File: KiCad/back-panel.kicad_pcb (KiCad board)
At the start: 2 copper layers, 93.3 x 69.3 mm, 4 parts

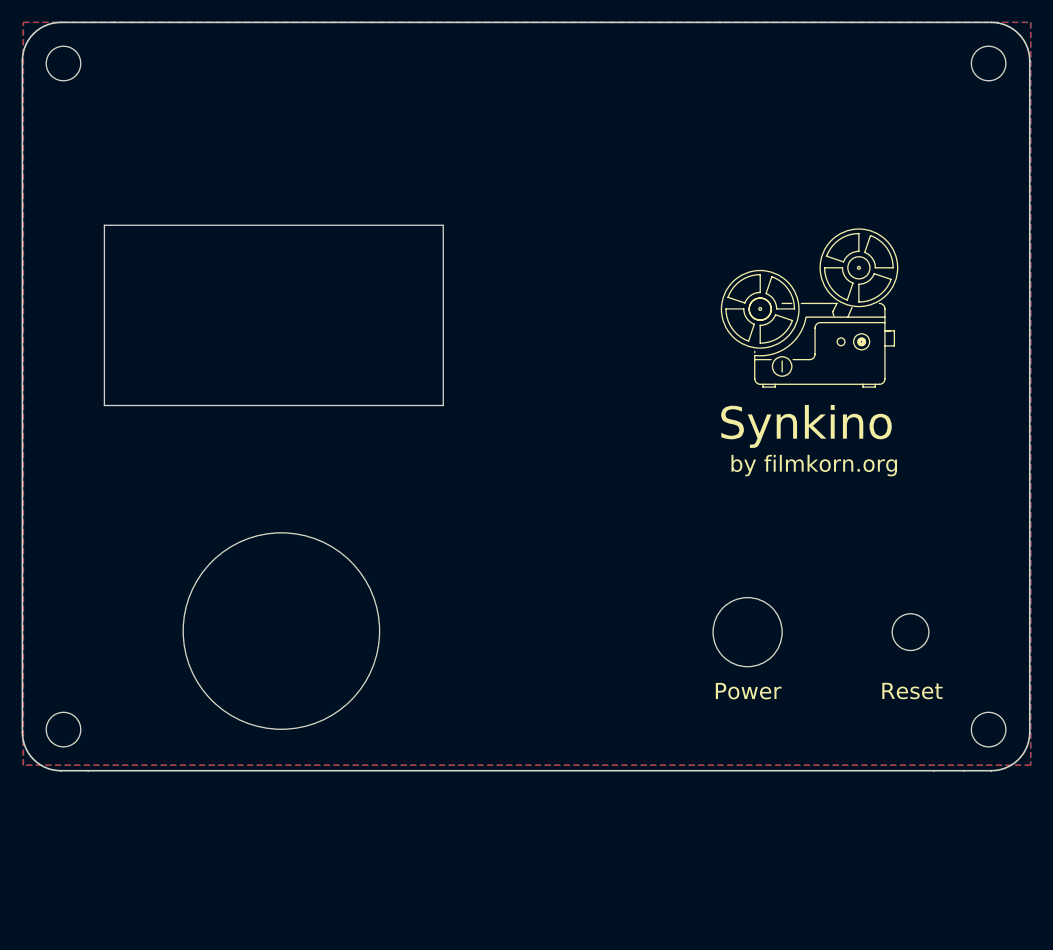
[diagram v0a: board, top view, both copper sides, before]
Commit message: Adding Battery Holder, Battery connector
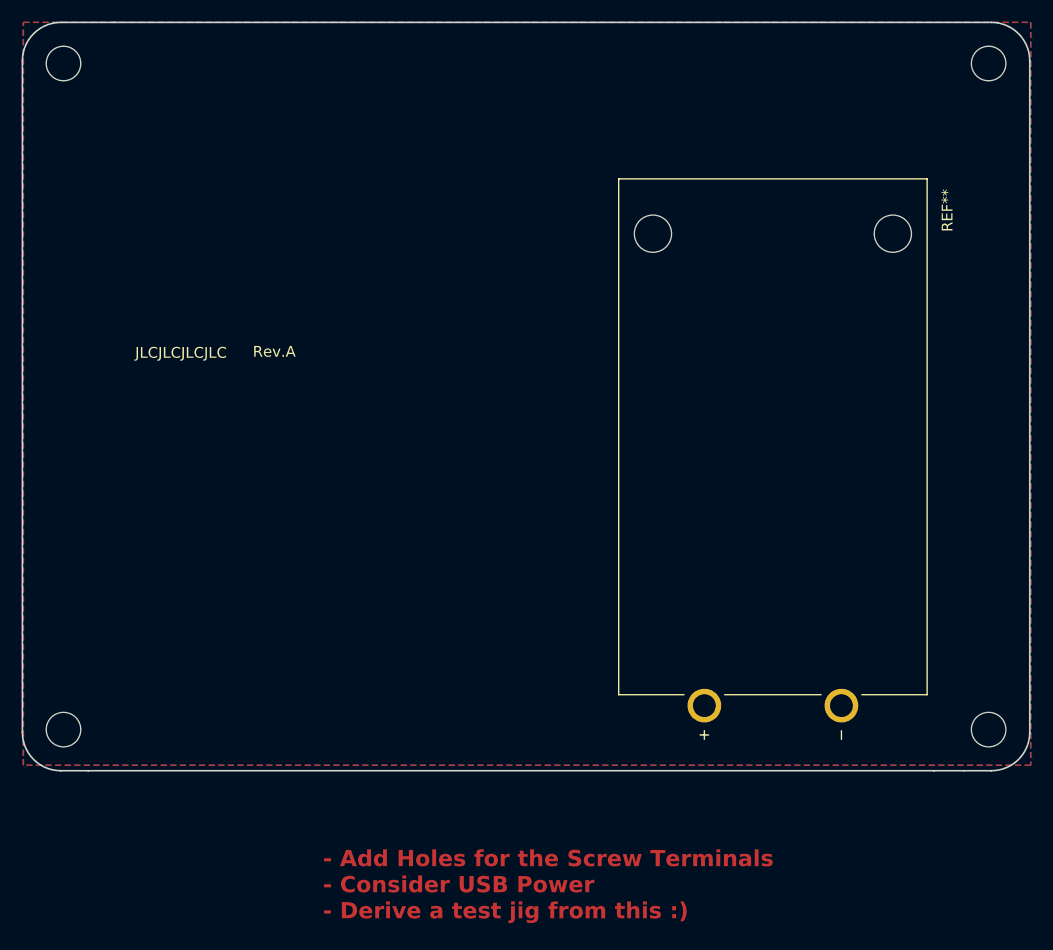
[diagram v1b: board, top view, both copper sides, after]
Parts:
- added REF**: BAT_1291-66-glued, Peacemans Teile:BAT_1291-66-glued, F.Cu at (165.4, 98.3)
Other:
- outline, holes or cut-outs redrawn
- board text added: "- Add Holes for the Screw Terminals - Consider USB Power - Derive a test jig from this :)"
- board text added: "Rev.A"
- board text removed: "Power"
- board text removed: "Reset"
- board text removed: "Rev.C"
- board text removed: "Synkino"
- board text removed: "by filmkorn.org"

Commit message: Adding screw holes to reach sensor's terminal blocks
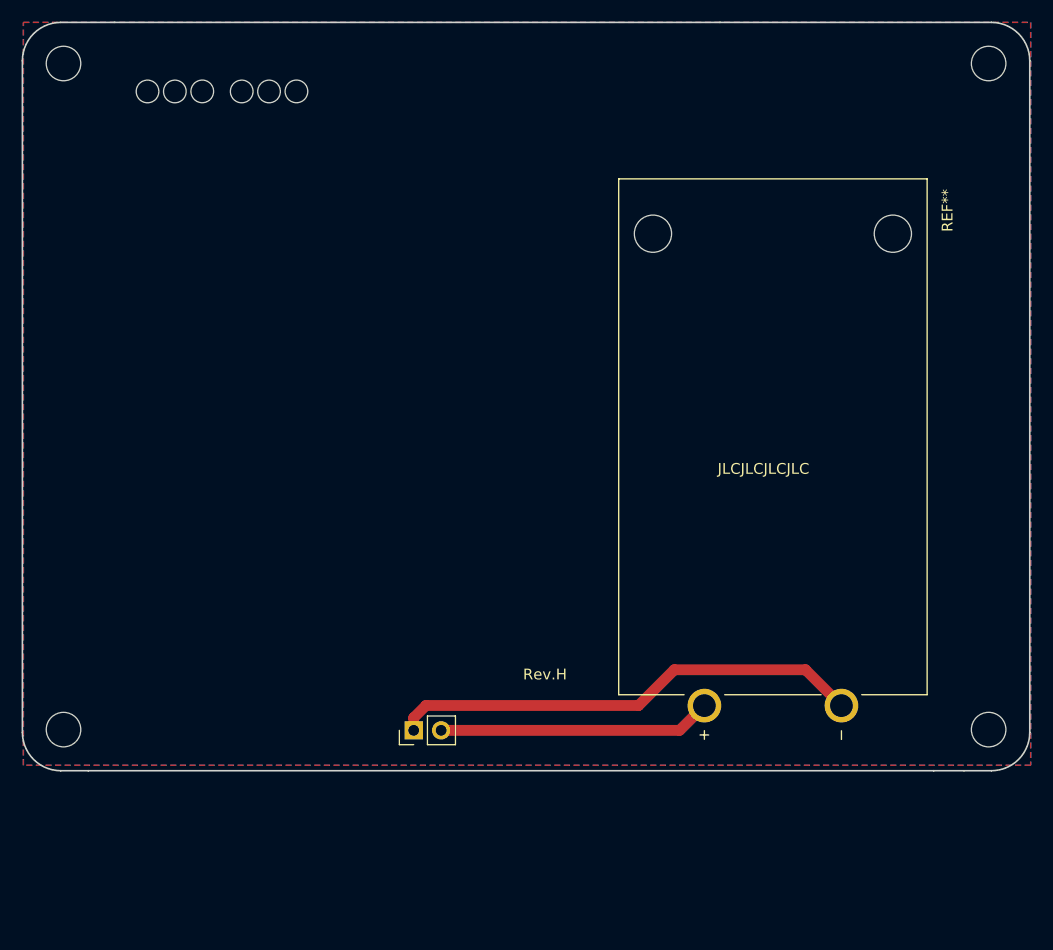
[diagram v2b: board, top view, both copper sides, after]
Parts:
- added J14: Pwr Pins, Connector_PinHeader_2.54mm:PinHeader_1x02_P2.54mm_Vertical, F.Cu at (132.1, 125.5)
- added REF**: MountingHole_2.1mm_just_hole, Peacemans Teile:MountingHole_2.1mm_just_hole, F.Cu at (112.5, 66.3)
- added REF**: MountingHole_2.1mm_just_hole, Peacemans Teile:MountingHole_2.1mm_just_hole, F.Cu at (118.7, 66.3)
- added REF**: MountingHole_2.1mm_just_hole, Peacemans Teile:MountingHole_2.1mm_just_hole, F.Cu at (116.2, 66.3)
- added REF**: MountingHole_2.1mm_just_hole, Peacemans Teile:MountingHole_2.1mm_just_hole, F.Cu at (107.5, 66.3)
- added REF**: MountingHole_2.1mm_just_hole, Peacemans Teile:MountingHole_2.1mm_just_hole, F.Cu at (110.0, 66.3)
- added REF**: MountingHole_2.1mm_just_hole, Peacemans Teile:MountingHole_2.1mm_just_hole, F.Cu at (121.2, 66.3)
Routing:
- net (no net): track 0.00 -> 69.4 mm
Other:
- board text added: "+"
- board text added: "-"
- board text added: "- Consider other Power Concepts - Order ~19 mm PIn headers - Derive a test jig from this :)"
- board text added: "Impulse"
- board text added: "Rev.H"
- board text added: "Startmark"
- board text added: "^"
- board text removed: "- Add Holes for the Screw Terminals - Consider USB Power - Derive a test jig from this :)"
- board text removed: "Rev.A"

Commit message: Adding a GND plane to the back panel
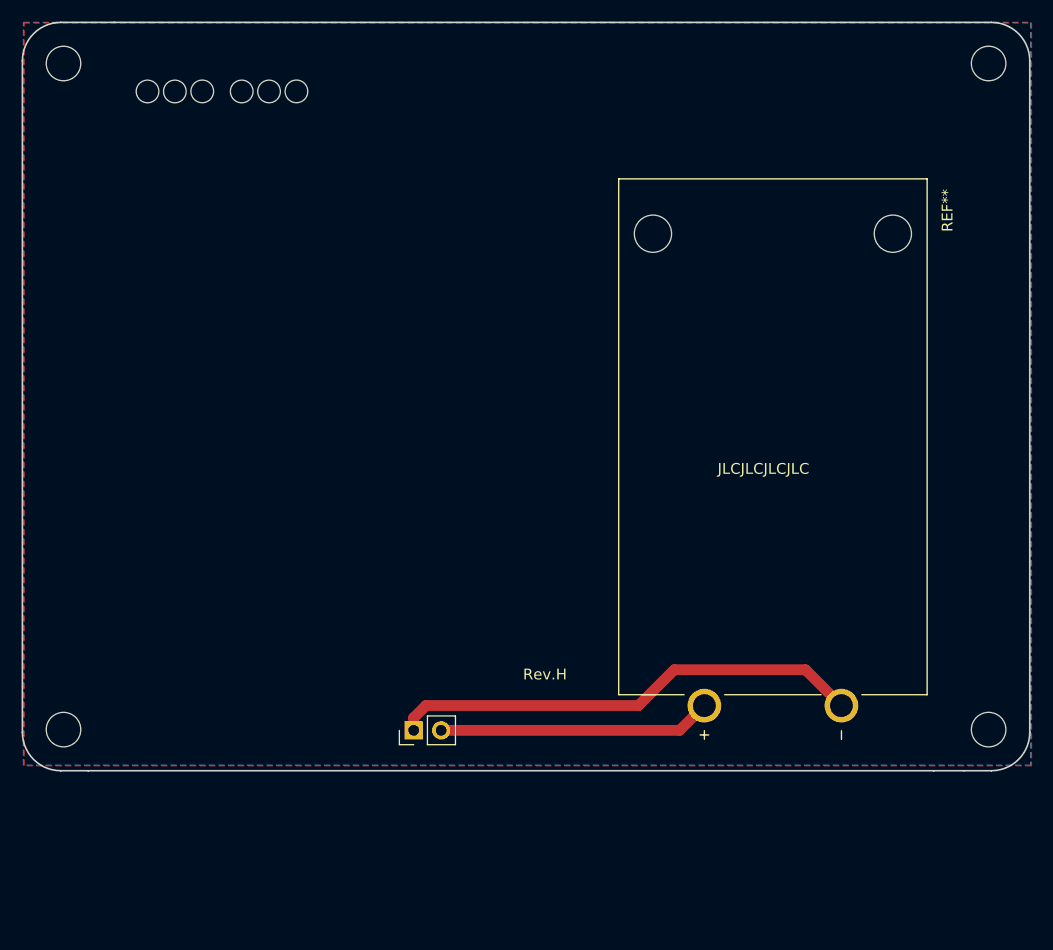
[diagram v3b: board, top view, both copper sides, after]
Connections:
- J14 pad 1: (no net) -> GND
- REF** pad N: (no net) -> GND
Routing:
- net GND: track 0.00 -> 69.4 mm
- net (no net): track 69.4 -> 0.00 mm
- added copper zone on B.Cu, net GND
- removed copper zone on B.Cu, net (none)
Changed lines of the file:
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@@
 	)
 	(net 0 "")
+	(net 1 "GND")
 	(footprint "Peacemans Teile:MountingHole_2.1mm_just_hole"
 		(layer "F.Cu")
@@
 			(layers "*.Cu" "*.Mask")
 			(remove_unused_layers no)
+			(net 1 "GND")
 			(pinfunction "Pin_1")
 			(pintype "passive")
@@
 			(layers "*.Cu" "*.Mask")
 			(remove_unused_layers no)
+			(net 1 "GND")
 			(solder_mask_margin 0.102)
 		)
@@
 		(width 1)
 		(layer "F.Cu")
-		(net 0)
+		(net 1)
 	)
 	(segment
@@
 		(width 1)
 		(layer "F.Cu")
-		(net 0)
+		(net 1)
 	)
 	(segment
@@
 		(width 1)
 		(layer "F.Cu")
-		(net 0)
+		(net 1)
 	)
 	(segment
@@
 		(width 1)
 		(layer "F.Cu")
-		(net 0)
+		(net 1)
 	)
 	(segment
@@
 		(width 1)
 		(layer "F.Cu")
-		(net 0)
+		(net 1)
 	)
 	(segment
@@
 		(width 1)
 		(layer "F.Cu")
-		(net 0)
+		(net 1)
 	)
 	(segment
@@
 		(width 1)
 		(layer "F.Cu")
-		(net 0)
+		(net 1)
 	)
 	(segment
@@
 		(width 1)
 		(layer "F.Cu")
-		(net 0)
+		(net 1)
 	)
 	(zone
@@
 		(polygon
 			(pts
-				(xy 189.275 59.9) (xy 189.275 128.734) (xy 95.93 128.734) (xy 95.93 59.9)
+				(xy 189.357 59.944) (xy 189.357 128.778) (xy 96.012 128.778) (xy 96.012 59.944)
 			)
 		)
 	)
 	(zone
-		(net 0)
-		(net_name "")
+		(net 1)
+		(net_name "GND")
 		(layer "B.Cu")
 		(hatch edge 0.508)
